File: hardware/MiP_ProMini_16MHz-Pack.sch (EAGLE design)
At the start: 52 parts, among them J2 AVR_ISP, Q1 16MHZ, U1 ATMEGA328, U2 MIC5205-5.0, U3 TS3USB221A, U4 MIC5205-3.3

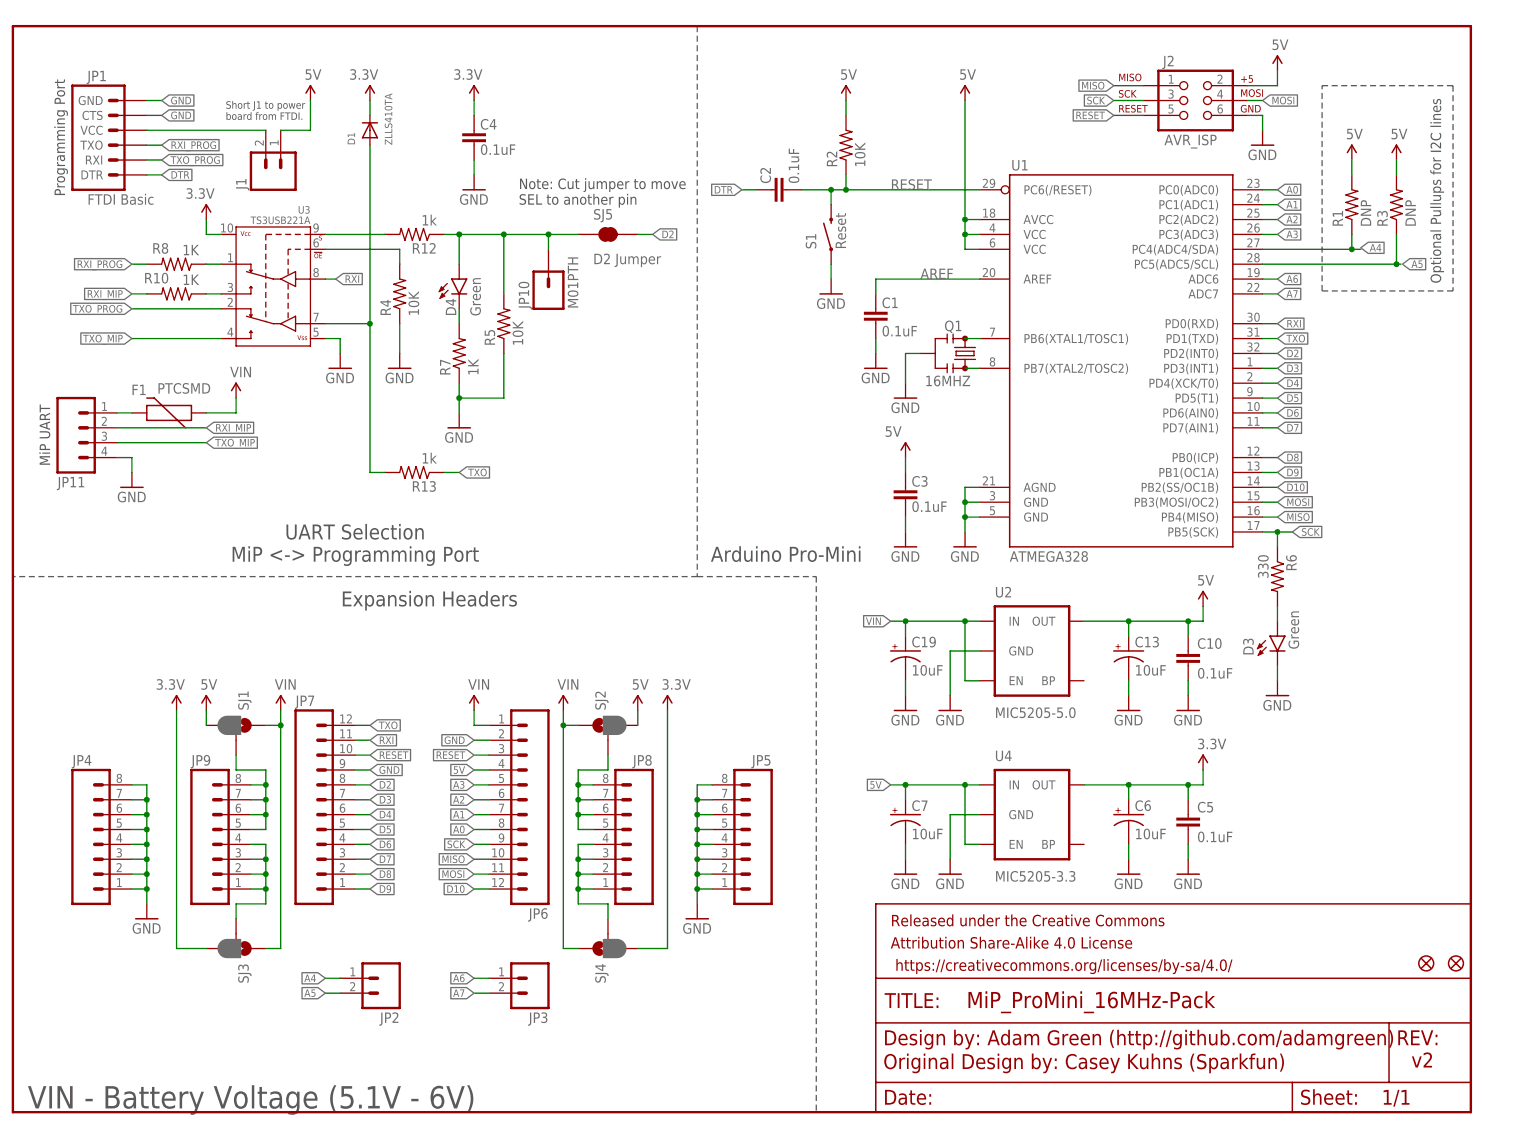
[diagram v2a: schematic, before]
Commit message: Initial layout complete
No more air wires to route and passes OSHPark DRC.

Important notes:
* I had to move the A6/A7 1x2 jumper block to move the AVR up higher on
  the board. This was done to make more room for larger passives and an
  extra voltage regulator lower on the board.
* I ended up removing the AVR-ISP port since I couldn't fit it on the
  left side of the board where it would have been easy to route.
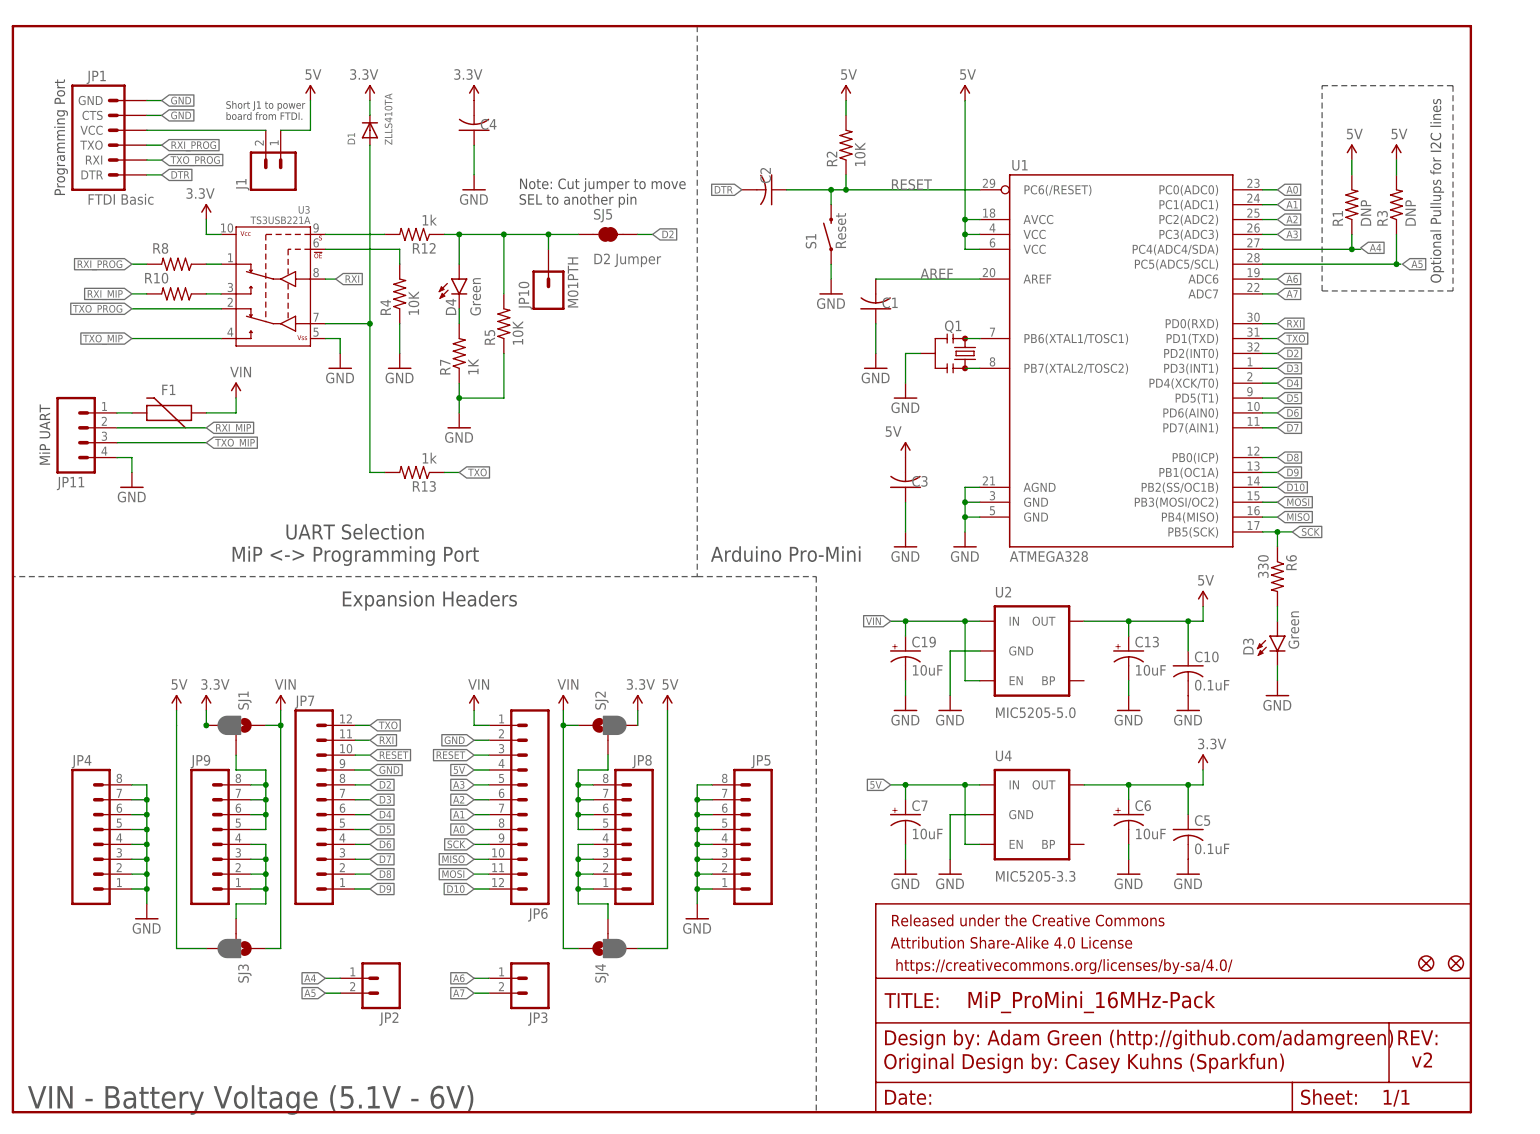
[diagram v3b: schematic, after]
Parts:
- removed J2: AVR_ISP, SparkFun-Connectors:AVR_SPI_PRG_6PTH
- C1, C10, C2, C3, C4, C5: device SparkFun-Capacitors:0.1UF-25V(+80/-20%)(0603) -> rcl:C-USC0805
- F1: value PTCSMD -> PTCCUSTOM; device SparkFun-PowerIC:PTCSMD -> adam_custom:PTCCUSTOM
- Q1: device SparkFun-FreqCtrl:RESONATOR16MHZ -> adam_custom:RESONATORMURATA_16MHZ
- R1, R2, R3: device SparkFun:RESISTOR0603-RES -> rcl:R-US_R0805
- R10, R7, R8: device SparkFun-Resistors:1KOHM1/10W1%(0603) -> rcl:R-US_R0805
- R12, R13, R4, R5: device SparkFun-Resistors:10KOHM1/10W1%(0603)0603 -> rcl:R-US_R0805
- R6: device SparkFun-Resistors:330OHM1/10W1%(0603) -> rcl:R-US_R0805
- S1: device SparkFun-Electromechanical:SWITCH-MOMENTARY-2SMD -> adam_custom:SWITCH-MOMENTARY-NOSMD
- U3: device SparkFun-AnalogIC:TS3USB221A -> adam_custom:TS3USB221ACUSTOM
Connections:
- net 3.3V: now also SJ1.3, SJ2.3; no longer SJ3.3, SJ4.3
- net 5V: now also SJ3.3, SJ4.3; no longer J2.2, SJ1.3, SJ2.3
- net GND: no longer J2.6
- net MISO: no longer J2.1
- net MOSI: no longer J2.4
- net RESET: no longer J2.5
- net SCK: no longer J2.3
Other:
- moved on the sheet: C1, C10, C2, C3, C4, C5

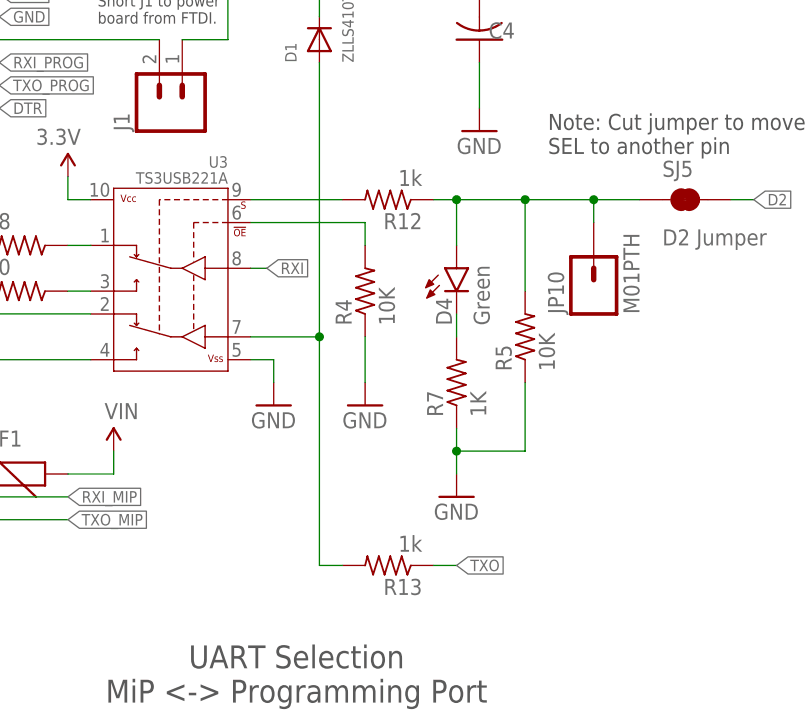
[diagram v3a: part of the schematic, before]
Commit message: Use consistent case for 1K resistor value
I had used 1k in some places and 1K in others so that 2 different items
showed up in BOM.
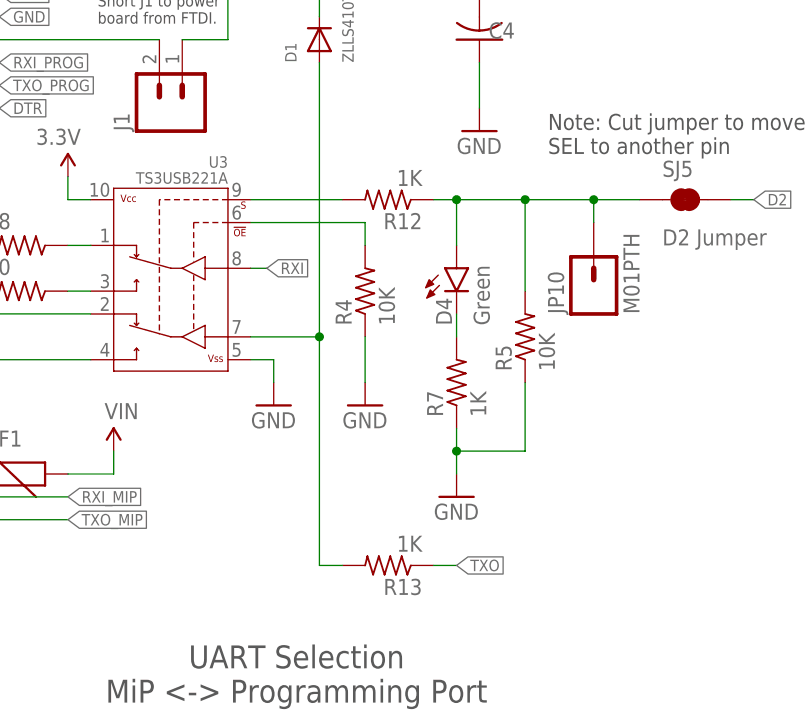
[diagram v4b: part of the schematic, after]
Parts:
- R12, R13: value 1k -> 1K
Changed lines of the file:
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@@
 <part name="J1" library="SparkFun-Connectors" deviceset="M02" device="PTH"/>
 <part name="P+10" library="SparkFun-Aesthetics" deviceset="5V" device="" value="5V"/>
-<part name="R12" library="rcl" deviceset="R-US_" device="R0805" value="1k"/>
+<part name="R12" library="rcl" deviceset="R-US_" device="R0805" value="1K"/>
 <part name="D1" library="adafruit" deviceset="DIODE" device="SOD-323F" value="ZLLS410TA"/>
 <part name="P+12" library="SparkFun-Aesthetics" deviceset="3.3V" device="" value="3.3V"/>
-<part name="R13" library="rcl" deviceset="R-US_" device="R0805" value="1k"/>
+<part name="R13" library="rcl" deviceset="R-US_" device="R0805" value="1K"/>
 <part name="R10" library="rcl" deviceset="R-US_" device="R0805" value="1K"/>
 <part name="P+4" library="SparkFun-Aesthetics" deviceset="5V" device="" value="5V"/>

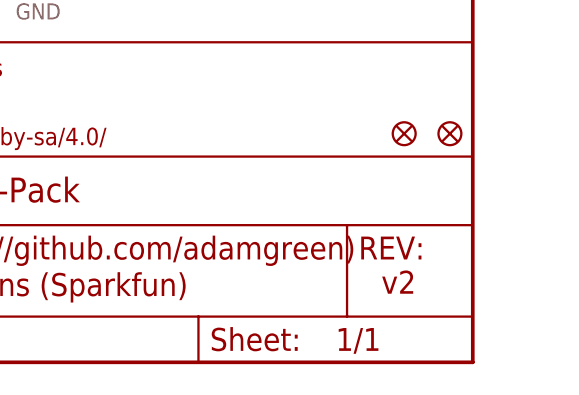
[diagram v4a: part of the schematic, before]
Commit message: Update schematic version to 3
I should have done this earlier when I removed the AVR-ISP header,
etc.
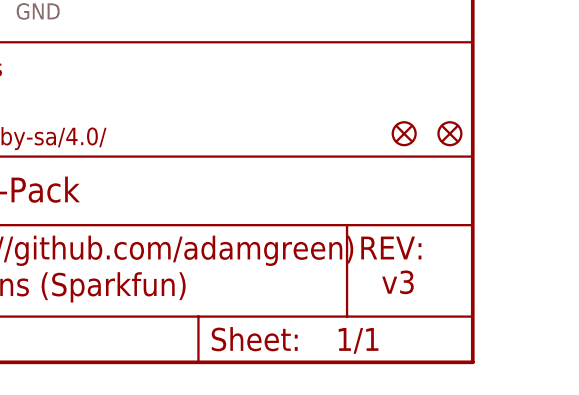
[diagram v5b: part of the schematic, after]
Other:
- note added: "v3"
- note removed: "v2"
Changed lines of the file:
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@@
 <text x="243.84" y="141.478" size="1.778" layer="97" rot="R90">Optional Pullups for I2C lines</text>
 <text x="166.37" y="11.43" size="2.54" layer="94">Adam Green (http://github.com/adamgreen)</text>
-<text x="238.76" y="7.62" size="2.54" layer="94">v2</text>
+<text x="238.76" y="7.62" size="2.54" layer="94">v3</text>
 <text x="86.36" y="154.94" size="1.778" layer="97">Note: Cut jumper to move
 SEL to another pin</text>
